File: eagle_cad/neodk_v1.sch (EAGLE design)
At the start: 71 parts, among them J1 SWD, J2 Power 5V..10V DC, J3 FC68131, J4 S2B-XH-A(LF)(SN), J5 S2B-XH-A(LF)(SN), Q1 IRLML6344TRPBF, Q2 IRLML6344TRPBF, Q3 PMV50EPEAR, SW2 FSMRA6JH, U1 SGM61410XN6G/TR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

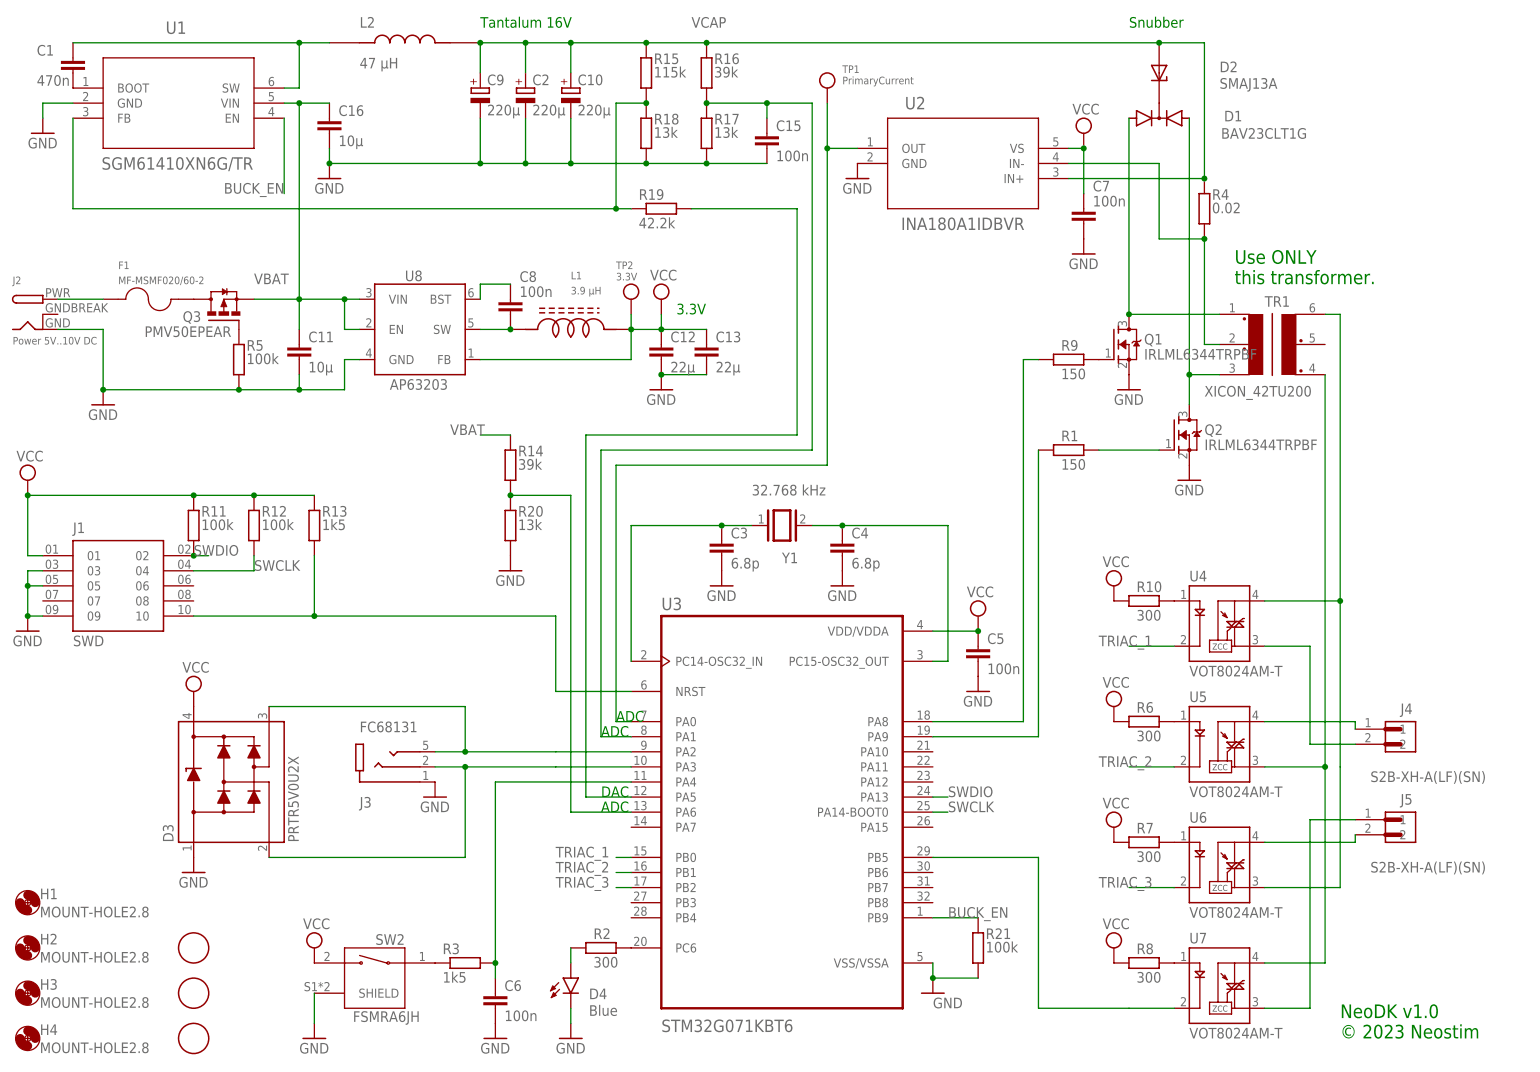
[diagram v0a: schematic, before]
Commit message: Generate pulses.
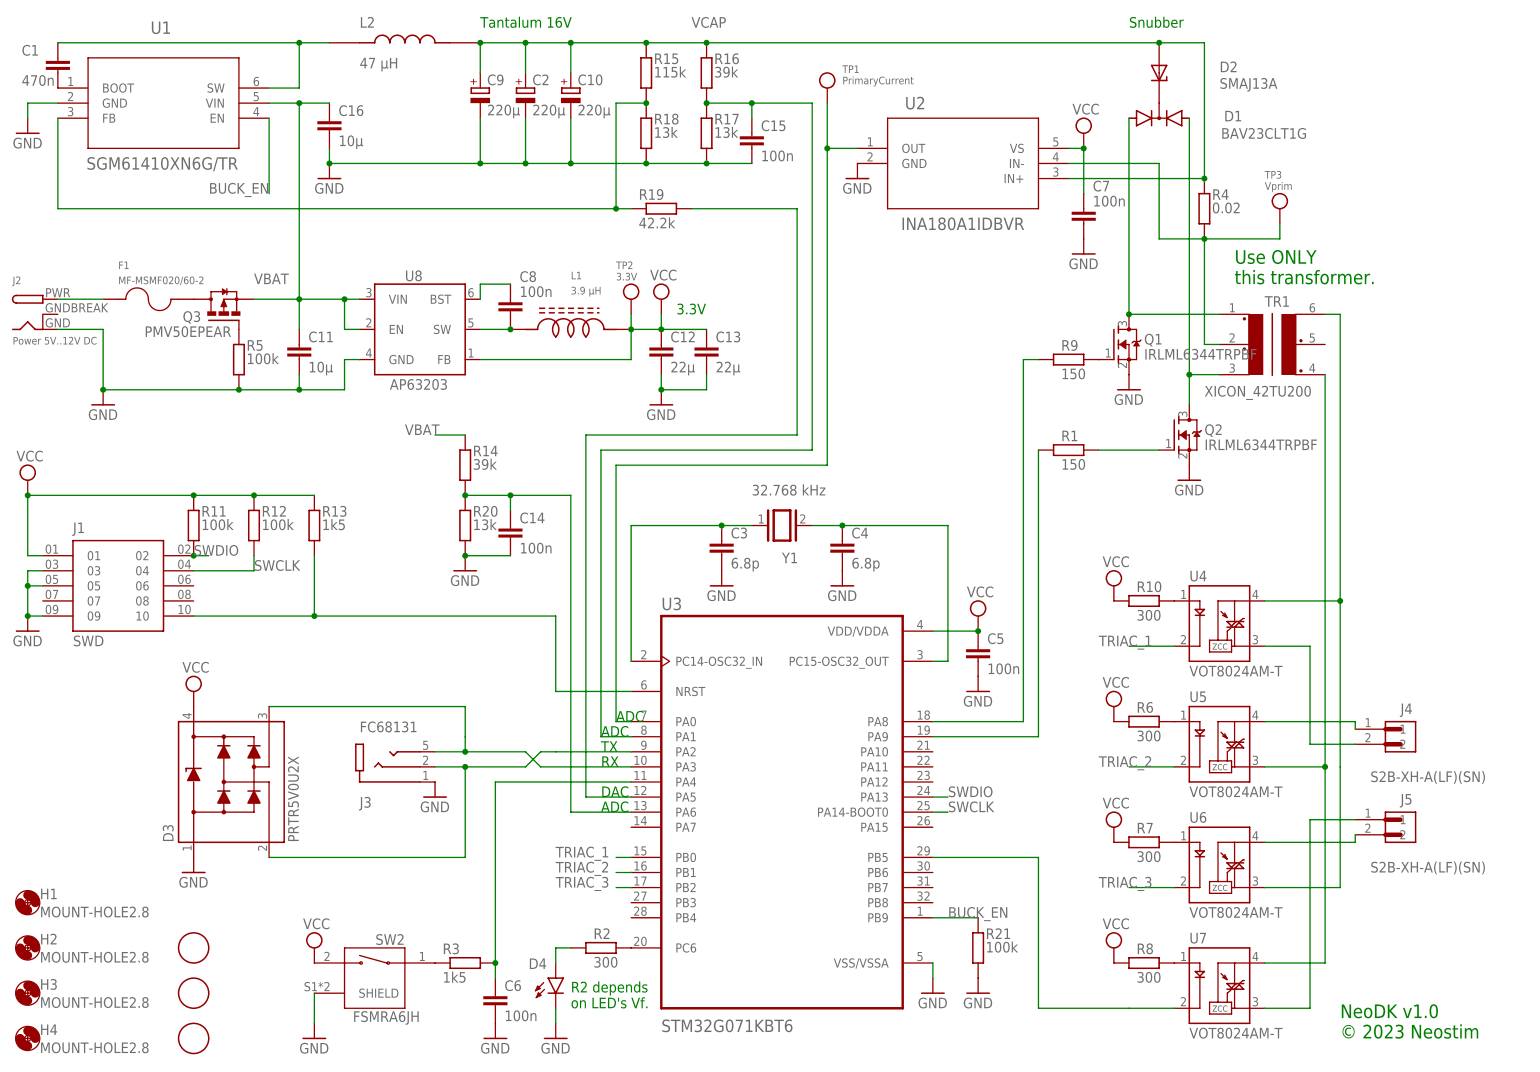
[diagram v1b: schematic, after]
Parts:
- added C14: 100n, rcl:C-EUC0603
- added TP3: Vprim, microbuilder:TESTPOINTROUND1MM
- D4: value Blue -> (none)
- J2: value Power 5V..10V DC -> Power 5V..12V DC
- U3: device STM32G0B1KET6:STM32G0B1KET6 -> STM32G071KBT6:STM32G071KBT6
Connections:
- net GND: now also C14.2
- net N$26: now also U3.PA3; no longer U3.PA2
- net N$29: now also U3.PA2; no longer U3.PA3
- net N$34: now also C14.1
- net N$9: now also TP3.P$1
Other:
- note added: "R2 depends on LED's Vf."
- note added: "RX"
- note added: "TX"
- moved on the sheet: C1, C15, D4, R14, R20, U1

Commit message: More firmware and Eagle board file.
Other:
- note added: "A"
- note added: "B"
- note added: "C"
- note added: "D"
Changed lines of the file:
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@@
 <text x="88.9" y="-25.4" size="1.778" layer="91">TX</text>
 <text x="88.9" y="-27.94" size="1.778" layer="91">RX</text>
+<text x="228.6" y="-25.4" size="1.778" layer="91">A</text>
+<text x="228.6" y="-22.86" size="1.778" layer="91">B</text>
+<text x="228.6" y="-40.64" size="1.778" layer="91">C</text>
+<text x="228.6" y="-38.1" size="1.778" layer="91">D</text>
 </plain>
 <instances>
@@
 <instance part="J4" gate="G$1" x="223.52" y="-22.86" smashed="yes">
 <attribute name="NAME" x="223.52" y="-19.05" size="1.778" layer="95"/>
-<attribute name="VALUE" x="218.44" y="-30.48" size="1.778" layer="96"/>
+<attribute name="VALUE" x="215.9" y="-30.48" size="1.778" layer="96"/>
 </instance>
 <instance part="J5" gate="G$1" x="223.52" y="-38.1" smashed="yes">
 <attribute name="NAME" x="223.52" y="-34.29" size="1.778" layer="95"/>
-<attribute name="VALUE" x="218.44" y="-45.72" size="1.778" layer="96"/>
+<attribute name="VALUE" x="215.9" y="-45.72" size="1.778" layer="96"/>
 </instance>
 <instance part="D3" gate="G$1" x="25.4" y="-30.48" smashed="yes" rot="R90">

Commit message: Prep for serial comms and pulse sequencer.
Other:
- note added: "NeoDK v1.0 © 2023, 2024 Neostim"
- note removed: "NeoDK v1.0 © 2023 Neostim"
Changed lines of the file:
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@@
 <text x="195.58" y="53.34" size="2.286" layer="91" ratio="12">Use ONLY
 this transformer.</text>
-<text x="213.36" y="-73.66" size="2.286" layer="91" ratio="10">NeoDK v1.0
-© 2023 Neostim</text>
+<text x="132.08" y="48.26" size="2.286" layer="91" ratio="10">NeoDK v1.0
+© 2023, 2024 Neostim</text>
 <text x="91.44" y="-20.32" size="1.778" layer="91">ADC</text>
 <text x="88.9" y="-22.86" size="1.778" layer="91">ADC</text>

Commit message: Updated schematic and board.
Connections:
- net VCC: no longer D3.VCC
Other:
- note added: "NeoDK v1.1 © 2023, 2024 Neostim"
- note removed: "NeoDK v1.0 © 2023, 2024 Neostim"
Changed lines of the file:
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@@
 <part name="D3" library="PRTR5V0U2X" deviceset="PRTR5V0U2X" device=""/>
 <part name="GND5" library="supply1" library_urn="urn:adsk.eagle:library:371" deviceset="GND" device=""/>
-<part name="SUPPLY3" library="supply2" library_urn="urn:adsk.eagle:library:372" deviceset="VCC" device=""/>
 <part name="R21" library="rcl" library_urn="urn:adsk.eagle:library:334" deviceset="R-EU_" device="R0603" package3d_urn="urn:adsk.eagle:package:23555/3" value="100k"/>
 <part name="GND18" library="supply1" library_urn="urn:adsk.eagle:library:371" deviceset="GND" device=""/>
@@
 <text x="195.58" y="53.34" size="2.286" layer="91" ratio="12">Use ONLY
 this transformer.</text>
-<text x="132.08" y="48.26" size="2.286" layer="91" ratio="10">NeoDK v1.0
+<text x="132.08" y="48.26" size="2.286" layer="91" ratio="10">NeoDK v1.1
 © 2023, 2024 Neostim</text>
 <text x="91.44" y="-20.32" size="1.778" layer="91">ADC</text>
@@
 <instance part="GND5" gate="1" x="20.32" y="-45.72" smashed="yes">
 <attribute name="VALUE" x="17.78" y="-48.26" size="1.778" layer="96"/>
-</instance>
-<instance part="SUPPLY3" gate="G$1" x="20.32" y="-15.24" smashed="yes">
-<attribute name="VALUE" x="18.415" y="-12.065" size="1.778" layer="96"/>
 </instance>
 <instance part="R21" gate="G$1" x="152.4" y="-58.42" smashed="yes" rot="R90">
@@
 <wire x1="93.98" y1="45.72" x2="99.06" y2="45.72" width="0.1524" layer="91"/>
 </segment>
-<segment>
-<pinref part="D3" gate="G$1" pin="VCC"/>
-<pinref part="SUPPLY3" gate="G$1" pin="VCC"/>
-</segment>
 </net>
